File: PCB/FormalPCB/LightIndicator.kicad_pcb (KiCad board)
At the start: 2 copper layers, 51 x 52 mm, 38 parts, among them M2 Screw MountingHole_2.2mm_M2

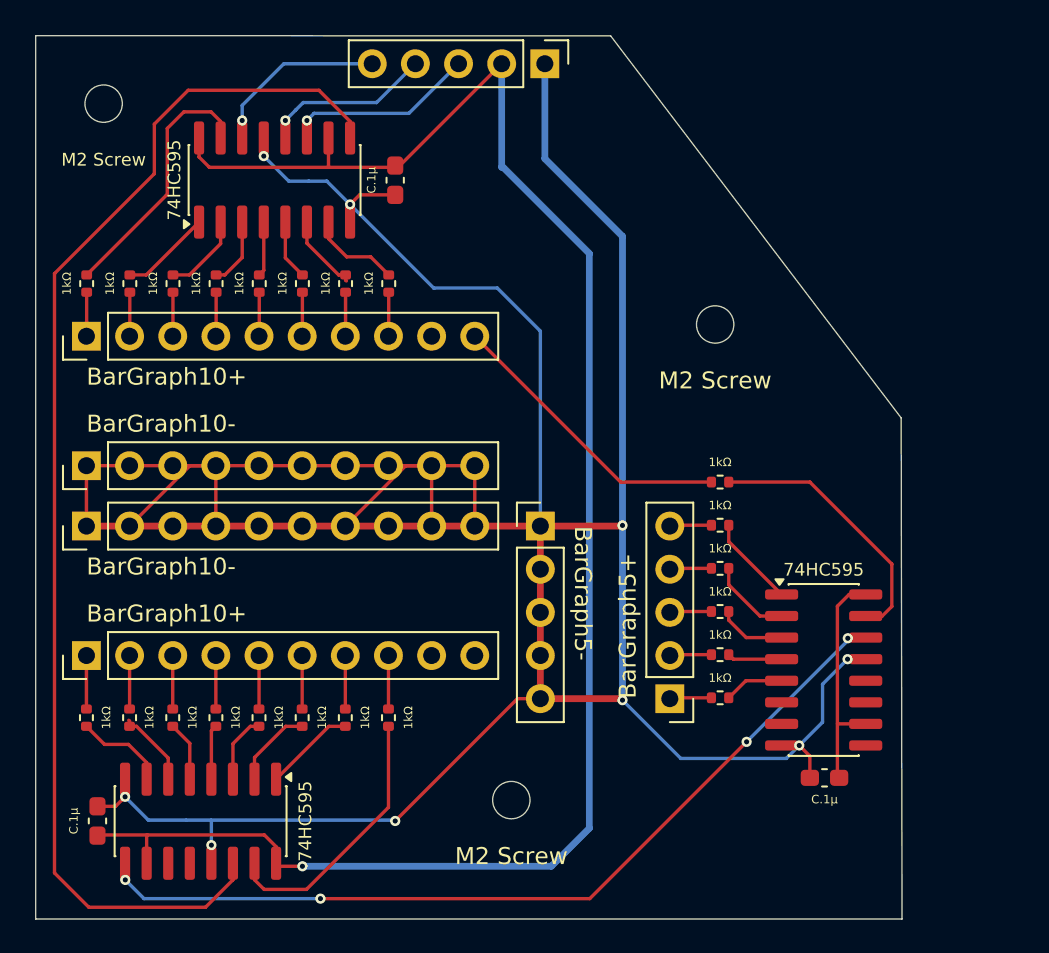
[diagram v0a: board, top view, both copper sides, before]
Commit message: Test SPI, regenerate IR code, complete PCB design
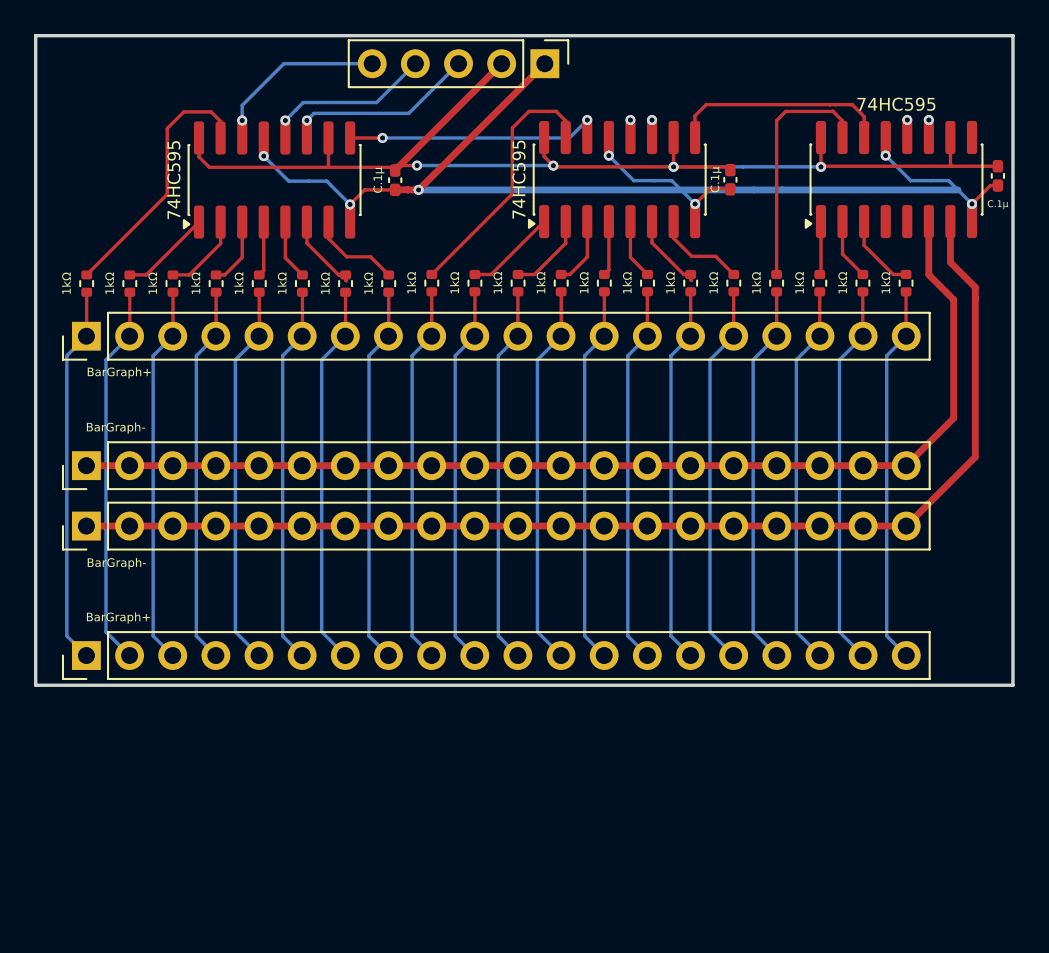
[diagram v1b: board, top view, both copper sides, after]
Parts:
- removed the 1kΩ at (5.53, 40.1)
- removed the 1kΩ at (40.3, 39.0)
- removed the 1kΩ at (20.8, 40.1)
- removed the 1kΩ at (40.3, 26.3)
- removed the 1kΩ at (40.3, 31.4)
- removed the 1kΩ at (40.3, 33.9)
- removed the 1kΩ at (8.07, 40.1)
- removed the 1kΩ at (18.2, 40.1)
- removed the 1kΩ at (40.3, 36.4)
- removed the 1kΩ at (2.99, 40.1)
- removed the 1kΩ at (15.7, 40.1)
- removed the 1kΩ at (10.6, 40.1)
- removed the 1kΩ at (40.3, 28.8)
- removed the 1kΩ at (13.1, 40.1)
- removed the 74HC595 at (9.71, 46.2)
- removed the 74HC595 at (46.4, 37.3)
- removed BarGraph5+, BarGraph5-: PinHeader_1x05_P2.54mm_Vertical, Connector_PinHeader_2.54mm:PinHeader_1x05_P2.54mm_Vertical
- removed the C.1μ at (46.4, 43.7)
- removed the C.1μ at (3.64, 46.2)
- removed M2 Screw: MountingHole_2.2mm_M2, MountingHole:MountingHole_2.2mm_M2 (x3)
- added 1kΩ: R_0402_1005Metric, Resistor_SMD:R_0402_1005Metric, F.Cu at (41.1, 14.6)
- added 1kΩ: R_0402_1005Metric, Resistor_SMD:R_0402_1005Metric, F.Cu at (36.0, 14.6)
- added 1kΩ: R_0402_1005Metric, Resistor_SMD:R_0402_1005Metric, F.Cu at (23.3, 14.6)
- added 1kΩ: R_0402_1005Metric, Resistor_SMD:R_0402_1005Metric, F.Cu at (25.9, 14.6)
- added 1kΩ: R_0402_1005Metric, Resistor_SMD:R_0402_1005Metric, F.Cu at (38.6, 14.6)
- added 1kΩ: R_0402_1005Metric, Resistor_SMD:R_0402_1005Metric, F.Cu at (46.2, 14.6)
- added 1kΩ: R_0402_1005Metric, Resistor_SMD:R_0402_1005Metric, F.Cu at (28.4, 14.6)
- added 1kΩ: R_0402_1005Metric, Resistor_SMD:R_0402_1005Metric, F.Cu at (51.2, 14.6)
- added 1kΩ: R_0402_1005Metric, Resistor_SMD:R_0402_1005Metric, F.Cu at (30.9, 14.6)
- added 1kΩ: R_0402_1005Metric, Resistor_SMD:R_0402_1005Metric, F.Cu at (48.7, 14.6)
- added 1kΩ: R_0402_1005Metric, Resistor_SMD:R_0402_1005Metric, F.Cu at (43.6, 14.6)
- added 1kΩ: R_0402_1005Metric, Resistor_SMD:R_0402_1005Metric, F.Cu at (33.5, 14.6)
- added 74HC595: SOIC-16_3.9x9.9mm_P1.27mm, Package_SO:SOIC-16_3.9x9.9mm_P1.27mm, F.Cu at (34.4, 8.47)
- added 74HC595: SOIC-16_3.9x9.9mm_P1.27mm, Package_SO:SOIC-16_3.9x9.9mm_P1.27mm, F.Cu at (50.7, 8.47)
- added C.1μ: C_0402_1005Metric_Pad0.74x0.62mm_HandSolder, Capacitor_SMD:C_0402_1005Metric_Pad0.74x0.62mm_HandSolder, F.Cu at (56.6, 8.26)
- added C.1μ: C_0402_1005Metric_Pad0.74x0.62mm_HandSolder, Capacitor_SMD:C_0402_1005Metric_Pad0.74x0.62mm_HandSolder, F.Cu at (40.9, 8.48)
- added G***: LOGO, Arnoll_Studio_Logo:Banner_Kicad, B.Cu at (27.2, 13.5)
- BarGraph+ (x2): renamed from BarGraph10+; value PinHeader_1x10_P2.54mm_Vertical -> PinHeader_1x20_P2.54mm_Vertical; footprint Connector_PinHeader_2.54mm:PinHeader_1x10_P2.54mm_Vertical -> Connector_PinHeader_2.54mm:PinHeader_1x20_P2.54mm_Vertical
- BarGraph- (x2): renamed from BarGraph10-; value PinHeader_1x10_P2.54mm_Vertical -> PinHeader_1x20_P2.54mm_Vertical; footprint Connector_PinHeader_2.54mm:PinHeader_1x10_P2.54mm_Vertical -> Connector_PinHeader_2.54mm:PinHeader_1x20_P2.54mm_Vertical
- C.1μ: value C_0603_1608Metric_Pad1.08x0.95mm_HandSolder -> C_0402_1005Metric_Pad0.74x0.62mm_HandSolder; footprint Capacitor_SMD:C_0603_1608Metric_Pad1.08x0.95mm_HandSolder -> Capacitor_SMD:C_0402_1005Metric_Pad0.74x0.62mm_HandSolder
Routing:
- net R-LED: track 82.4 -> 451.9 mm
- net 595Din: track 132.6 -> 37.1 mm, vias 5 -> 3
- net VCC: track 117.5 -> 69.5 mm, vias 1 -> 4
- net GND: track 223.0 -> 205.4 mm, vias 9 -> 7
- net 595Output: track 130.4 -> 118.9 mm
- net 595latch: vias 1 -> 3
- net 595CLK: vias 1 -> 3
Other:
- board size 51 x 52 mm -> 57.5 x 38.2 mm
